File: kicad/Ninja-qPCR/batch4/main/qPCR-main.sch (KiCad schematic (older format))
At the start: 38 parts, among them J1 Raspberry_Pi_3A_Plus_wpi, J2 Conn_01x03_Male, J3 Conn_01x01_Male, J4 Conn_01x01_Male, J5 Conn_02x03_Odd_Even, J6 Conn_02x03_Odd_Even, J7 Conn_02x03_Odd_Even, Q1 Q_NMOS_GSD, Q2 Q_NMOS_GSD, Q3 Q_NMOS_GSD, Q4 Q_NMOS_GSD, Q5 Q_NMOS_GSD, Q6 Q_NMOS_GSD, SW1 TACTILE_4

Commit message: add workflow
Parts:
- removed BODY1, LED1, LID_2X1: Conn_02x05, Ninja-qPCR:Con_2x05, symbol Ninja-qPCR:Conn_02x05
- removed PHOTO1: Conn_01x14_Male, Pin_Headers:Pin_Header_Straight_1x14_Pitch2.54mm, symbol Connector:Conn_01x14_Male
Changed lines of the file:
@@
 Wire Wire Line
 	2150 2950 2000 2950
-Text GLabel 9950 4700 0    50   Input ~ 0
-GND
-Wire Wire Line
-	9950 4700 10150 4700
-Wire Wire Line
-	10150 4800 9950 4800
-Wire Wire Line
-	9950 4900 10150 4900
-Wire Wire Line
-	10150 5000 9950 5000
-Wire Wire Line
-	9950 5100 10150 5100
-Wire Wire Line
-	10150 5200 9950 5200
-Wire Wire Line
-	9950 5300 10150 5300
-Wire Wire Line
-	10150 5400 9950 5400
-Wire Wire Line
-	9950 5500 10150 5500
-$Comp
-L Ninja-qPCR:Conn_02x05 LED1
-U 1 1 5F7E3B13
-P 10200 3400
-AR Path="/5F7E3B13" Ref="LED1"  Part="1"
-AR Path="/5F708CA1/5F7E3B13" Ref="LED?"  Part="1"
-F 0 "LED1" H 10600 3100 50  0000 C CNN
-F 1 "Conn_02x05" H 10800 3000 50  0000 C CNN
-F 2 "Ninja-qPCR:Con_2x05" H 10000 3500 50  0001 C CNN
-F 3 "" H 10000 3500 50  0001 C CNN
-	1    10200 3400
-	1    0    0    -1
-$EndComp
-Text GLabel 9750 3600 0    50   Input ~ 0
-GND
-Text GLabel 9750 3700 0    50   Input ~ 0
-PD_REF_PWM
-Text GLabel 9750 3800 0    50   Input ~ 0
-LED_LAT
-Text GLabel 9750 4000 0    50   Input ~ 0
-LED_SPI_MOSI
-Text GLabel 9750 4100 0    50   Input ~ 0
-SPI_MISO
-Text GLabel 9750 4200 0    50   Input ~ 0
-I2C_SCL
-Text GLabel 9750 4300 0    50   Input ~ 0
-I2C_SDA
-Wire Wire Line
-	9750 4300 10000 4300
-Wire Wire Line
-	9750 4200 10000 4200
-Wire Wire Line
-	9750 4100 10000 4100
-Wire Wire Line
-	9750 4000 10000 4000
-Wire Wire Line
-	9750 3900 10000 3900
-Wire Wire Line
-	9750 3800 10000 3800
-Wire Wire Line
-	9750 3700 10000 3700
-Wire Wire Line
-	9750 3600 10000 3600
-Wire Wire Line
-	9750 3500 10000 3500
-Wire Wire Line
-	9750 3400 10000 3400
-Text GLabel 9950 5100 0    50   Input ~ 0
-PD_MUX_GPIO5
-Text GLabel 9950 5200 0    50   Input ~ 0
-PD_MUX_GPIO4
-Text GLabel 9950 5400 0    50   Input ~ 0
-PD_MUX_GPIO2
-Text GLabel 9950 5300 0    50   Input ~ 0
-PD_MUX_GPIO3
-Text GLabel 9950 5500 0    50   Input ~ 0
-PD_MUX_GPIO1
-Text GLabel 9950 5600 0    50   Input ~ 0
-PD_REF_PWM
-Text GLabel 9950 5700 0    50   Input ~ 0
-ADC_DRDY
-Text GLabel 9950 5800 0    50   Input ~ 0
-I2C_SCL
-Text GLabel 9950 5900 0    50   Input ~ 0
-I2C_SDA
-Wire Wire Line
-	10150 5600 9950 5600
-Wire Wire Line
-	10150 5700 9950 5700
-Wire Wire Line
-	10150 5800 9950 5800
-Wire Wire Line
-	10150 5900 9950 5900
 Text GLabel 3700 3150 2    50   Input ~ 0
 THERM_AIR
-Text GLabel 9950 6000 0    50   Input ~ 0
-THERM_WELL
-Wire Wire Line
-	9950 6000 10150 6000
 Text GLabel 3700 3250 2    50   Input ~ 0
 THERM_LID1
 Text GLabel 3700 3350 2    50   Input ~ 0
 THERM_LID2
-$Comp
-L Ninja-qPCR:Conn_02x05 BODY?
-U 1 1 5F7E3B97
-P 10200 950
-AR Path="/5F58C19F/5F7E3B97" Ref="BODY?"  Part="1"
-AR Path="/5F7E3B97" Ref="BODY1"  Part="1"
-AR Path="/5F708CA1/5F7E3B97" Ref="BODY?"  Part="1"
-F 0 "BODY1" H 10519 561 50  0000 L CNN
-F 1 "Conn_02x05" H 10519 470 50  0000 L CNN
-F 2 "Ninja-qPCR:Con_2x05" H 10000 1050 50  0001 C CNN
-F 3 "" H 10000 1050 50  0001 C CNN
-	1    10200 950
-	1    0    0    -1
-$EndComp
-$Comp
-L Ninja-qPCR:Conn_02x05 LID_2X?
-U 1 1 5F7E3B9D
-P 10200 2150
-AR Path="/5F58C19F/5F7E3B9D" Ref="LID_2X?"  Part="1"
-AR Path="/5F7E3B9D" Ref="LID_2X1"  Part="1"
-AR Path="/5F708CA1/5F7E3B9D" Ref="LID_2X?"  Part="1"
-F 0 "LID_2X1" H 10519 1761 50  0000 L CNN
-F 1 "Conn_02x05" H 10519 1670 50  0000 L CNN
-F 2 "Ninja-qPCR:Con_2x05" H 10000 2250 50  0001 C CNN
-F 3 "" H 10000 2250 50  0001 C CNN
-	1    10200 2150
-	1    0    0    -1
-$EndComp
-Text GLabel 9850 1050 0    50   Input ~ 0
-BODY_HEATER1B
-Text GLabel 9850 1150 0    50   Input ~ 0
-THERM_WELL
-Text GLabel 9850 1250 0    50   Input ~ 0
-FAN_BLACK_GND1
-Text GLabel 9850 1450 0    50   Input ~ 0
-GND
-Text GLabel 9850 1550 0    50   Input ~ 0
-FAN_BLACK_GND2
-Text GLabel 9850 1650 0    50   Input ~ 0
-THERM_EXT3
-Text GLabel 9850 1850 0    50   Input ~ 0
-BODY_HEATER2B
-Wire Wire Line
-	10000 950  9850 950
-Wire Wire Line
-	9850 1050 10000 1050
-Wire Wire Line
-	10000 1150 9850 1150
-Wire Wire Line
-	9850 1250 10000 1250
-Wire Wire Line
-	10000 1350 9850 1350
-Wire Wire Line
-	9850 1450 10000 1450
-Wire Wire Line
-	10000 1550 9850 1550
-Wire Wire Line
-	9850 1650 10000 1650
-Wire Wire Line
-	10000 1750 9850 1750
-Wire Wire Line
-	9850 1850 10000 1850
-Text GLabel 9850 2250 0    50   Input ~ 0
-LID_HEATER1B
-Text GLabel 9850 3050 0    50   Input ~ 0
-LID_HEATER2B
-Text GLabel 9850 2350 0    50   Input ~ 0
-THERM_AIR
-Text GLabel 9850 2450 0    50   Input ~ 0
-THERM_EXT1
-Text GLabel 9850 2550 0    50   Input ~ 0
-THERM_LID1
-Text GLabel 9850 2650 0    50   Input ~ 0
-GND
-Text GLabel 9850 2750 0    50   Input ~ 0
-THERM_LID2
-Text GLabel 9850 2850 0    50   Input ~ 0
-THERM_EXT2
-Wire Wire Line
-	10000 2150 9850 2150
-Wire Wire Line
-	9850 2250 10000 2250
-Wire Wire Line
-	10000 2350 9850 2350
-Wire Wire Line
-	9850 2450 10000 2450
-Wire Wire Line
-	10000 2550 9850 2550
-Wire Wire Line
-	9850 2650 10000 2650
-Wire Wire Line
-	10000 2750 9850 2750
-Wire Wire Line
-	9850 2850 10000 2850
-Wire Wire Line
-	10000 2950 9850 2950
-Wire Wire Line
-	9850 3050 10000 3050
 Text GLabel 3700 2250 2    50   Input ~ 0
 SPI_SWITCH
@@
 Wire Wire Line
 	3650 1450 3700 1450
-$Comp
-L Connector:Conn_01x14_Male PHOTO1
-U 1 1 5F89D7B6
-P 10350 5300
-F 0 "PHOTO1" H 10200 5300 50  0000 R CNN
-F 1 "Conn_01x14_Male" H 10200 5200 50  0000 R CNN
-F 2 "Pin_Headers:Pin_Header_Straight_1x14_Pitch2.54mm" H 10350 5300 50  0001 C CNN
-F 3 "~" H 10350 5300 50  0001 C CNN
-	1    10350 5300
-	-1   0    0    -1
-$EndComp
 Wire Wire Line
 	8100 3350 7950 3350
@@
 	8200 3950 7950 3950
 NoConn ~ 2000 2250
-Text GLabel 9750 3900 0    50   Input ~ 0
-SPI_SCLK
 $Sheet
 S 5850 2650 850  250
@@
 Text HLabel 8600 6000 2    50   Input ~ 0
 VCC_LOGIC_PHOTO
-Text HLabel 9950 5000 0    50   Input ~ 0
-VCC_LOGIC_PHOTO
-Text HLabel 9750 3500 0    50   Input ~ 0
-VCC_LOGIC_LED
 $Comp
 L Connector_Generic:Conn_02x03_Odd_Even J6
@@
 Text GLabel 3700 1450 2    50   Input ~ 0
 5V
-Text GLabel 9750 3400 0    50   Input ~ 0
-5V
-Text GLabel 9950 4800 0    50   Input ~ 0
-+10V
-Text GLabel 9950 4900 0    50   Input ~ 0
--10V
 Text GLabel 7750 4750 0    50   Input ~ 0
 3V3_SENSE
@@
 Text GLabel 7750 6000 0    50   Input ~ 0
 3V3_REG
-Text GLabel 9850 950  0    50   Input ~ 0
-12V
-Text GLabel 9850 1350 0    50   Input ~ 0
-12V
-Text GLabel 9850 1750 0    50   Input ~ 0
-12V
-Text GLabel 9850 2150 0    50   Input ~ 0
-12V
-Text GLabel 9850 2950 0    50   Input ~ 0
-12V
 Wire Wire Line
 	4250 2900 4400 2900

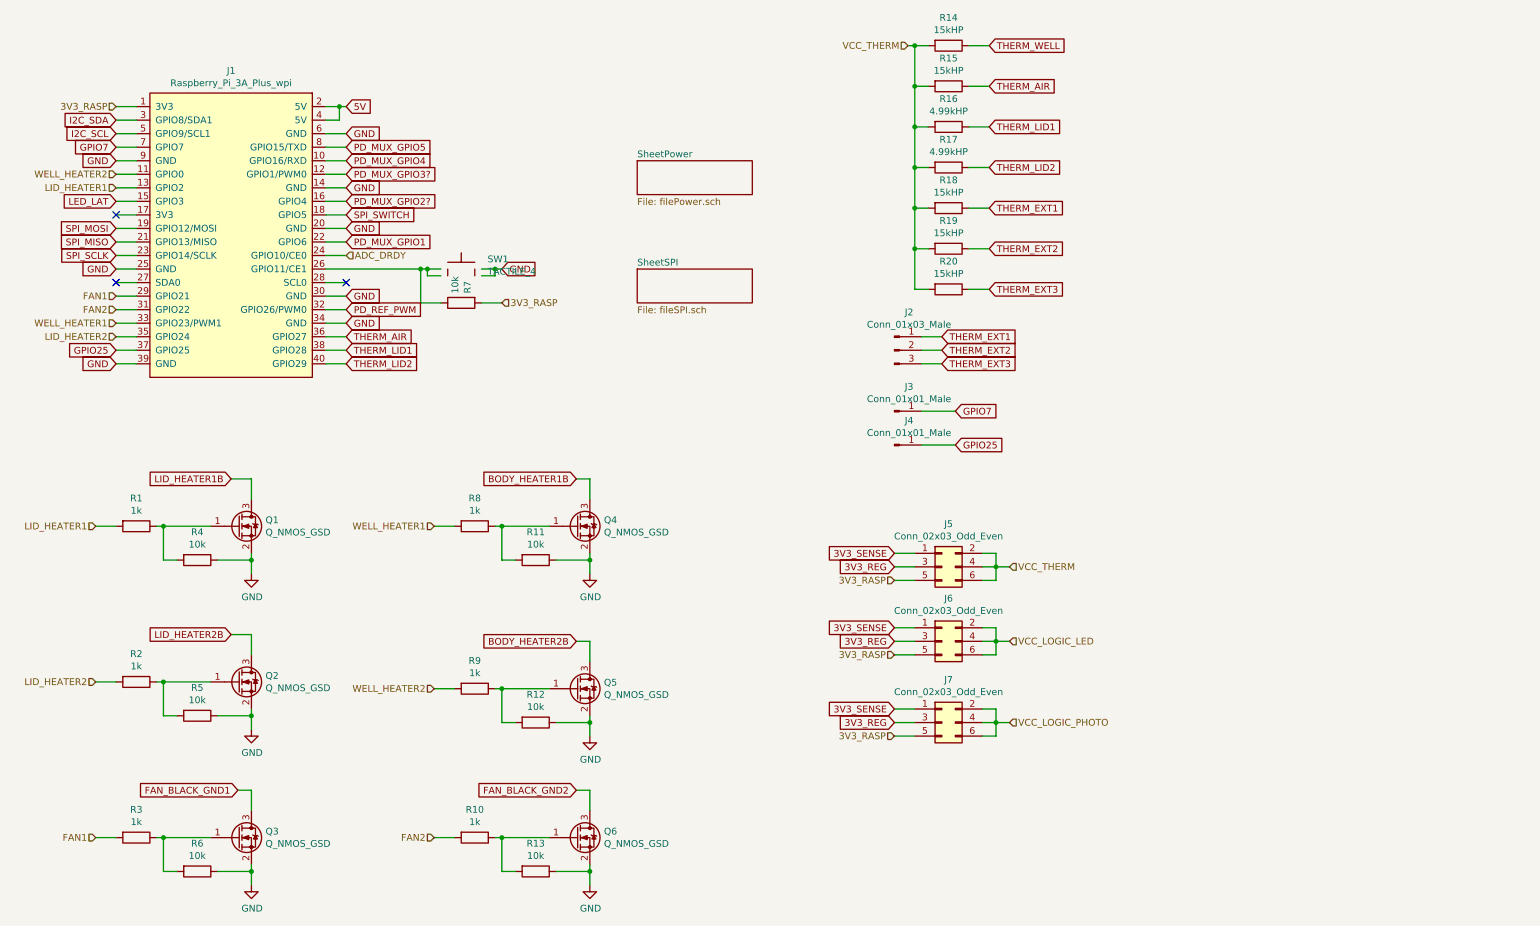
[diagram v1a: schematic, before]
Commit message: connect floating VCC_LOGIC to 3V3_RASP
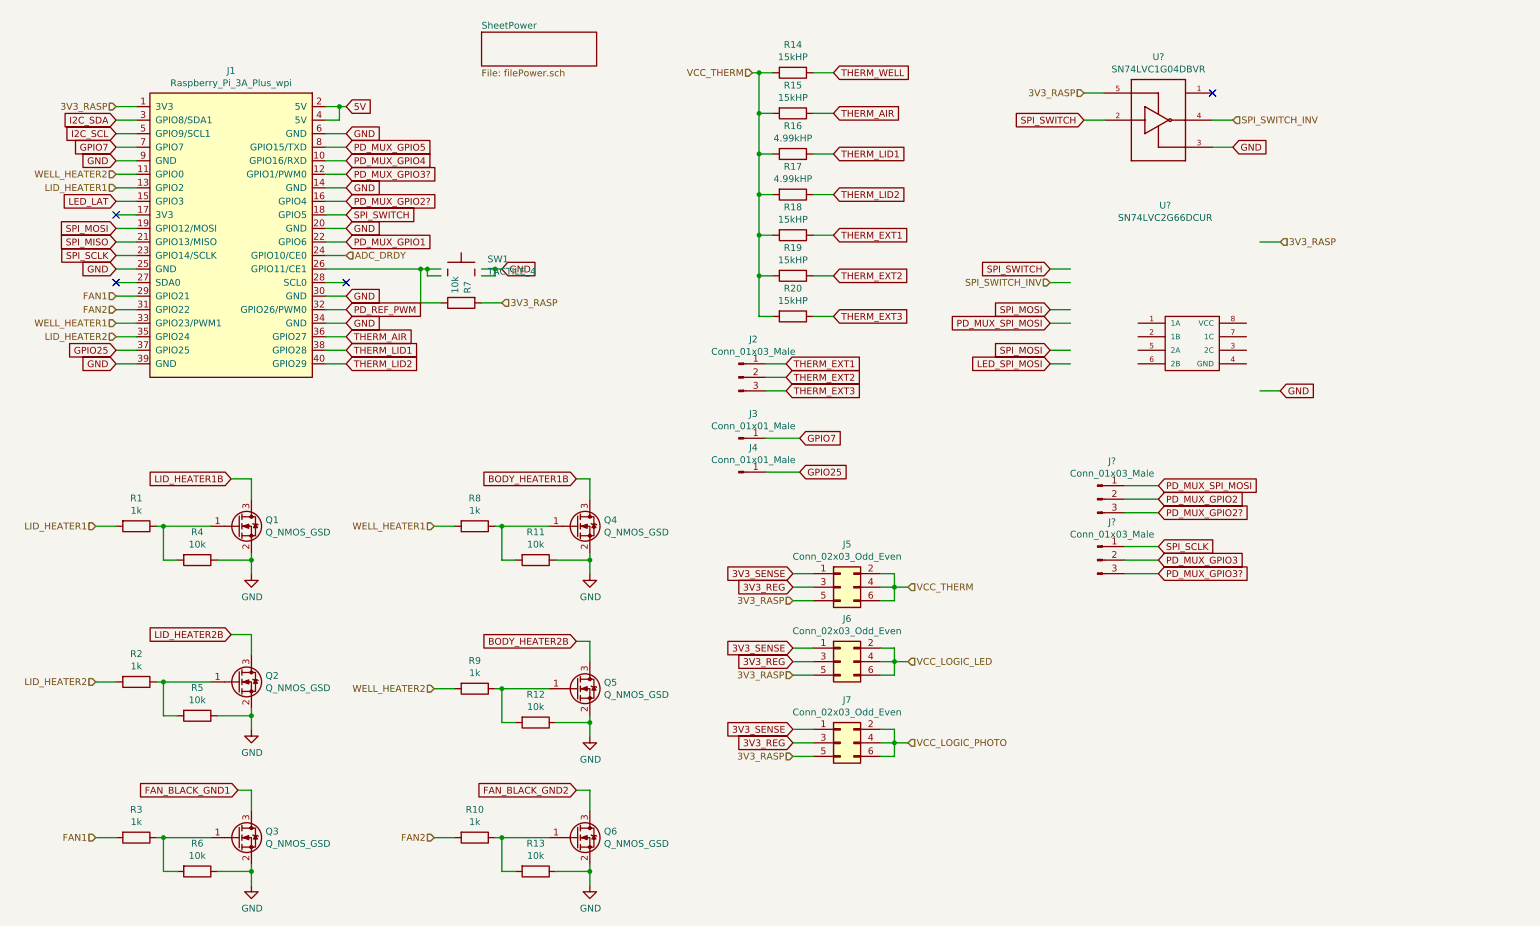
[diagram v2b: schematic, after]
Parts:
- added J? (x2): Conn_01x03_Male, Pin_Headers:Pin_Header_Straight_1x03_Pitch2.54mm, symbol Connector:Conn_01x03_Male
- added U?: SN74LVC1G04DBVR, Ninja-qPCR:SN74LVC1G04DBVR, symbol Ninja-qPCR:SN74LVC1G04DBVR
- added U?: SN74LVC2G66DCUR, Ninja-qPCR:SN74LVC2G66DCUR, symbol Ninja-qPCR:SN74LVC2G66DCUR
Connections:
- net labels added: LED_SPI_MOSI, PD_MUX_GPIO2, PD_MUX_GPIO3, PD_MUX_SPI_MOSI, SPI_SWITCH_INV
- wire segments 166 -> 184
- no-connect marks 3 -> 4
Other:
- moved on the sheet: J2, J3, J4, J5, J6, J7, R14, R15, R16, R17, R18, R19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

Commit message: buildup batch4/main
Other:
- moved on the sheet: J?, U?

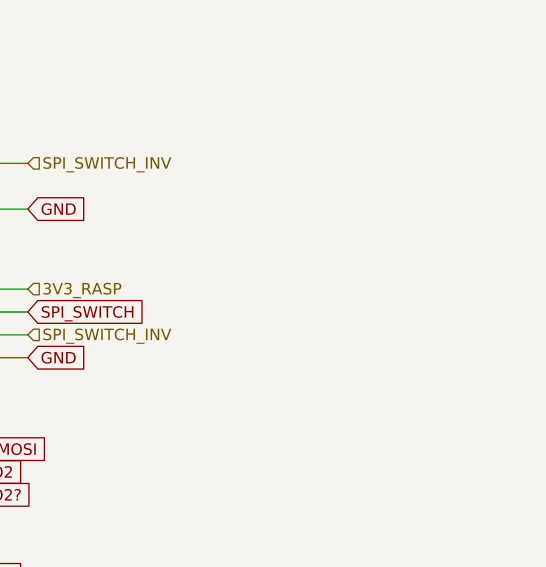
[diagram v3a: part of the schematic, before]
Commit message: use SPDT switch for SPI MOSI
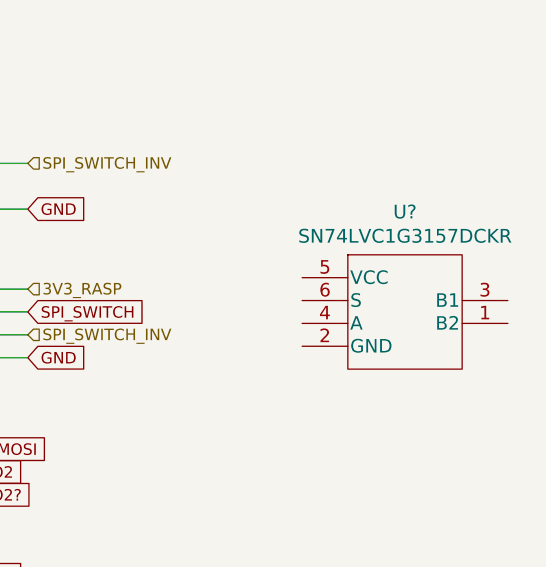
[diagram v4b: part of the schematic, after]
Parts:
- added U?: SN74LVC1G3157DCKR, DCK0006A_N, symbol Ninja-qPCR:SN74LVC1G3157DCKR
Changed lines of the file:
@@
 F1 "filePhotoSensing.sch" 50
 $EndSheet
+$Comp
+L Ninja-qPCR:SN74LVC1G3157DCKR U?
+U 1 1 602E131D
+P 11450 2050
+F 0 "U?" H 11900 2337 60  0000 C CNN
+F 1 "SN74LVC1G3157DCKR" H 11900 2231 60  0000 C CNN
+F 2 "DCK0006A_N" H 11900 1450 60  0001 C CNN
+F 3 "" H 12350 1750 60  0000 C CNN
+	1    11450 2050
+	1    0    0    -1
+$EndComp
 $EndSCHEMATC
